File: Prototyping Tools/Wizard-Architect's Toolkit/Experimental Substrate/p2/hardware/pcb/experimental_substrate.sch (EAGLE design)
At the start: 3 parts, among them J1 EURO_POWER

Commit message: Extreme improvements on stripboard v2
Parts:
- added D1, D2: SCHOTTKY_THT, SonicAthame:SCHOTTKY_THT
- added L1, L2: FERRITE_THT, SonicAthame:FERRITE_THT
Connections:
- new net N$10: J1.-12V, L2.P$1
- new net N$11: J1.+12V, L1.P$1
- new net N$8: D1.A, L1.P$2
- new net N$9: D2.C, L2.P$2
- net +12V: now also D1.C; no longer J1.+12V
- net -12V: now also D2.A; no longer J1.-12V
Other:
- note added: "2743005112"
- note added: "ESS106M063AE2EA"
- note added: "SB230TA"
- moved on the sheet: C1, C2
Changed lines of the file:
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@@
 <?xml version="1.0" encoding="utf-8"?>
 <!DOCTYPE eagle SYSTEM "eagle.dtd">
-<eagle version="9.5.0">
+<eagle version="9.6.2">
 <drawing>
 <settings>
@@
 <part name="J1" library="SonicAthame" library_urn="urn:adsk.eagle:library:22327399" deviceset="EURO_POWER" device="" package3d_urn="urn:adsk.eagle:package:26183621/4"/>
 <part name="FRAME1" library="SonicAthame" library_urn="urn:adsk.eagle:library:22327399" deviceset="FRAME_TABL_L" device=""/>
+<part name="D1" library="SonicAthame" library_urn="urn:adsk.eagle:library:22327399" deviceset="SCHOTTKY" device="_THT" package3d_urn="urn:adsk.eagle:package:26423854/3"/>
+<part name="D2" library="SonicAthame" library_urn="urn:adsk.eagle:library:22327399" deviceset="SCHOTTKY" device="_THT" package3d_urn="urn:adsk.eagle:package:26423854/3"/>
+<part name="L1" library="SonicAthame" library_urn="urn:adsk.eagle:library:22327399" deviceset="FERRITE" device="_THT" package3d_urn="urn:adsk.eagle:package:26183824/1"/>
+<part name="L2" library="SonicAthame" library_urn="urn:adsk.eagle:library:22327399" deviceset="FERRITE" device="_THT" package3d_urn="urn:adsk.eagle:package:26183824/1"/>
 </parts>
 <sheets>
 <sheet>
 <plain>
+<text x="205.994" y="128.778" size="1.778" layer="96">SB230TA</text>
+<text x="190.246" y="149.352" size="1.778" layer="96">2743005112</text>
+<text x="236.728" y="145.796" size="1.778" layer="96">ESS106M063AE2EA</text>
 </plain>
 <instances>
-<instance part="C1" gate="G$1" x="203.2" y="147.32" smashed="yes">
-<attribute name="NAME" x="204.216" y="147.955" size="1.778" layer="95"/>
-<attribute name="VALUE" x="204.216" y="143.129" size="1.778" layer="96"/>
-</instance>
-<instance part="C2" gate="G$1" x="203.2" y="132.08" smashed="yes">
-<attribute name="NAME" x="204.216" y="132.715" size="1.778" layer="95"/>
-<attribute name="VALUE" x="204.216" y="127.889" size="1.778" layer="96"/>
-</instance>
-<instance part="SUPPLY1" gate="+12V" x="198.12" y="152.4" smashed="yes">
-<attribute name="VALUE" x="198.12" y="155.321" size="1.778" layer="96" align="bottom-center"/>
-</instance>
-<instance part="SUPPLY2" gate="G$1" x="198.12" y="124.46" smashed="yes">
-<attribute name="VALUE" x="198.12" y="121.666" size="1.778" layer="96" align="top-center"/>
-</instance>
-<instance part="SUPPLY3" gate="PE" x="210.82" y="134.62" smashed="yes"/>
+<instance part="C1" gate="G$1" x="231.14" y="147.32" smashed="yes">
+<attribute name="NAME" x="232.156" y="147.955" size="1.778" layer="95"/>
+<attribute name="VALUE" x="232.156" y="143.129" size="1.778" layer="96"/>
+</instance>
+<instance part="C2" gate="G$1" x="231.14" y="132.08" smashed="yes">
+<attribute name="NAME" x="232.156" y="132.715" size="1.778" layer="95"/>
+<attribute name="VALUE" x="232.156" y="127.889" size="1.778" layer="96"/>
+</instance>
+<instance part="SUPPLY1" gate="+12V" x="226.06" y="152.4" smashed="yes">
+<attribute name="VALUE" x="226.06" y="155.321" size="1.778" layer="96" align="bottom-center"/>
+</instance>
+<instance part="SUPPLY2" gate="G$1" x="226.06" y="124.46" smashed="yes">
+<attribute name="VALUE" x="226.06" y="121.666" size="1.778" layer="96" align="top-center"/>
+</instance>
+<instance part="SUPPLY3" gate="PE" x="238.76" y="134.62" smashed="yes"/>
 <instance part="J1" gate="G$1" x="185.42" y="139.7" smashed="yes">
 <attribute name="NAME" x="177.927" y="147.828" size="1.778" layer="95"/>
-<attribute name="VALUE" x="177.927" y="130.048" size="1.778" layer="95"/>
+<attribute name="VALUE" x="175.387" y="130.048" size="1.778" layer="95"/>
 </instance>
 <instance part="FRAME1" gate="G$1" x="0" y="0" smashed="yes"/>
@@
 <attribute name="REV" x="391.16" y="6.35" size="2.54" layer="94"/>
 </instance>
+<instance part="D1" gate="G$1" x="208.28" y="144.78" smashed="yes">
+<attribute name="NAME" x="205.994" y="146.685" size="1.778" layer="95"/>
+<attribute name="VALUE" x="205.994" y="141.351" size="1.778" layer="96"/>
+</instance>
+<instance part="D2" gate="G$1" x="208.28" y="134.62" smashed="yes" rot="R180">
+<attribute name="NAME" x="205.994" y="136.525" size="1.778" layer="95"/>
+<attribute name="VALUE" x="205.994" y="131.191" size="1.778" layer="96"/>
+</instance>
+<instance part="L1" gate="G$1" x="198.12" y="144.78" smashed="yes">
+<attribute name="NAME" x="194.691" y="146.812" size="1.778" layer="95"/>
+</instance>
+<instance part="L2" gate="G$1" x="198.12" y="134.62" smashed="yes">
+<attribute name="NAME" x="194.691" y="136.652" size="1.778" layer="95"/>
+</instance>
 </instances>
 <busses>
@@
 <net name="+12V" class="0">
 <segment>
-<wire x1="190.5" y1="144.78" x2="198.12" y2="144.78" width="0.1524" layer="91"/>
-<wire x1="198.12" y1="144.78" x2="198.12" y2="149.86" width="0.1524" layer="91"/>
+<wire x1="226.06" y1="144.78" x2="226.06" y2="149.86" width="0.1524" layer="91"/>
 <pinref part="C1" gate="G$1" pin="+"/>
-<wire x1="198.12" y1="149.86" x2="203.2" y2="149.86" width="0.1524" layer="91"/>
+<wire x1="226.06" y1="149.86" x2="231.14" y2="149.86" width="0.1524" layer="91"/>
 <pinref part="SUPPLY1" gate="+12V" pin="+12V"/>
-<junction x="198.12" y="149.86"/>
+<junction x="226.06" y="149.86"/>
+<pinref part="D1" gate="G$1" pin="C"/>
+<wire x1="210.82" y1="144.78" x2="226.06" y2="144.78" width="0.1524" layer="91"/>
+</segment>
+</net>
+<net name="-12V" class="0">
+<segment>
+<wire x1="226.06" y1="134.62" x2="226.06" y2="127" width="0.1524" layer="91"/>
+<pinref part="C2" gate="G$1" pin="-"/>
+<wire x1="226.06" y1="127" x2="231.14" y2="127" width="0.1524" layer="91"/>
+<pinref part="SUPPLY2" gate="G$1" pin="-12V"/>
+<junction x="226.06" y="127"/>
+<pinref part="D2" gate="G$1" pin="A"/>
+<wire x1="210.82" y1="134.62" x2="226.06" y2="134.62" width="0.1524" layer="91"/>
+</segment>
+</net>
+<net name="GND" class="0">
+<segment>
+<wire x1="190.5" y1="139.7" x2="231.14" y2="139.7" width="0.1524" layer="91"/>
+<pinref part="C1" gate="G$1" pin="-"/>
+<wire x1="231.14" y1="139.7" x2="231.14" y2="142.24" width="0.1524" layer="91"/>
+<pinref part="C2" gate="G$1" pin="+"/>
+<wire x1="231.14" y1="139.7" x2="231.14" y2="134.62" width="0.1524" layer="91"/>
+<junction x="231.14" y="139.7"/>
+<pinref part="SUPPLY3" gate="PE" pin="GND"/>
+<wire x1="231.14" y1="139.7" x2="238.76" y2="139.7" width="0.1524" layer="91"/>
+<wire x1="238.76" y1="139.7" x2="238.76" y2="137.16" width="0.1524" layer="91"/>
+<pinref part="J1" gate="G$1" pin="GND"/>
+</segment>
+</net>
+<net name="N$8" class="0">
+<segment>
+<pinref part="D1" gate="G$1" pin="A"/>
+<wire x1="203.2" y1="144.78" x2="205.74" y2="144.78" width="0.1524" layer="91"/>
+<pinref part="L1" gate="G$1" pin="P$2"/>
+</segment>
+</net>
+<net name="N$9" class="0">
+<segment>
+<pinref part="D2" gate="G$1" pin="C"/>
+<wire x1="205.74" y1="134.62" x2="203.2" y2="134.62" width="0.1524" layer="91"/>
+<pinref part="L2" gate="G$1" pin="P$2"/>
+</segment>
+</net>
+<net name="N$10" class="0">
+<segment>
+<pinref part="J1" gate="G$1" pin="-12V"/>
+<wire x1="193.04" y1="134.62" x2="190.5" y2="134.62" width="0.1524" layer="91"/>
+<pinref part="L2" gate="G$1" pin="P$1"/>
+</segment>
+</net>
+<net name="N$11" class="0">
+<segment>
 <pinref part="J1" gate="G$1" pin="+12V"/>
-</segment>
-</net>
-<net name="-12V" class="0">
-<segment>
-<wire x1="190.5" y1="134.62" x2="198.12" y2="134.62" width="0.1524" layer="91"/>
-<wire x1="198.12" y1="134.62" x2="198.12" y2="127" width="0.1524" layer="91"/>
-<pinref part="C2" gate="G$1" pin="-"/>
-<wire x1="198.12" y1="127" x2="203.2" y2="127" width="0.1524" layer="91"/>
-<pinref part="SUPPLY2" gate="G$1" pin="-12V"/>
-<junction x="198.12" y="127"/>
-<pinref part="J1" gate="G$1" pin="-12V"/>
-</segment>
-</net>
-<net name="GND" class="0">
-<segment>
-<wire x1="190.5" y1="139.7" x2="203.2" y2="139.7" width="0.1524" layer="91"/>
-<pinref part="C1" gate="G$1" pin="-"/>
-<wire x1="203.2" y1="139.7" x2="203.2" y2="142.24" width="0.1524" layer="91"/>
-<pinref part="C2" gate="G$1" pin="+"/>
-<wire x1="203.2" y1="139.7" x2="203.2" y2="134.62" width="0.1524" layer="91"/>
-<junction x="203.2" y="139.7"/>
-<pinref part="SUPPLY3" gate="PE" pin="GND"/>
-<wire x1="203.2" y1="139.7" x2="210.82" y2="139.7" width="0.1524" layer="91"/>
-<wire x1="210.82" y1="139.7" x2="210.82" y2="137.16" width="0.1524" layer="91"/>
-<pinref part="J1" gate="G$1" pin="GND"/>
-</segment>
-</net>
+<wire x1="193.04" y1="144.78" x2="190.5" y2="144.78" width="0.1524" layer="91"/>
+<pinref part="L1" gate="G$1" pin="P$1"/>
+</segment>
+</net>

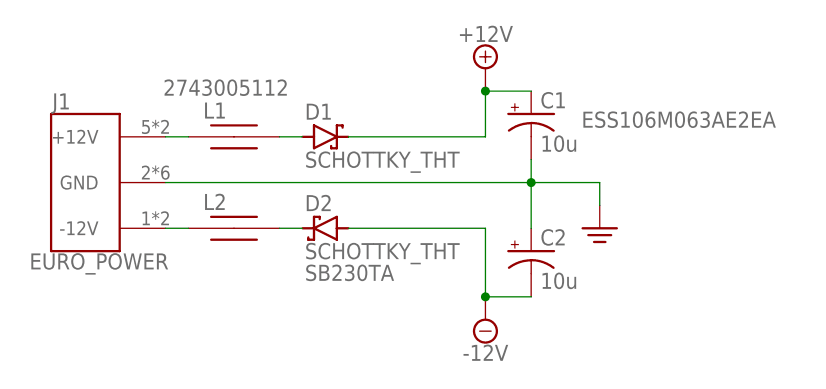
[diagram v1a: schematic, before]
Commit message: Cleaner schematic layout
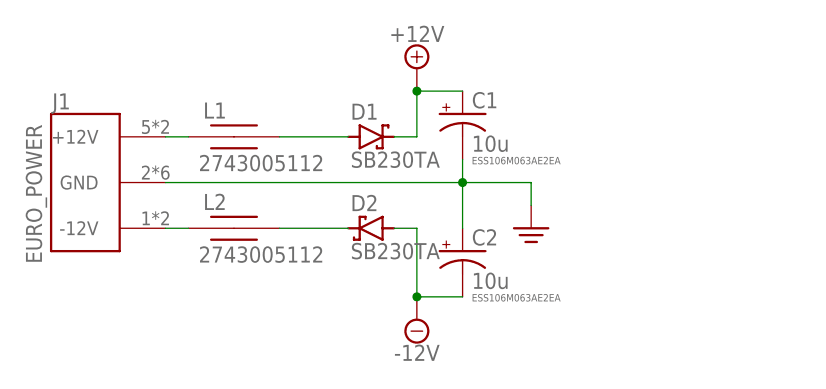
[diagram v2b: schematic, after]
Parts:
- D1, D2: value SCHOTTKY_THT -> SB230TA
- L1, L2: value FERRITE_THT -> 2743005112
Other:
- note removed: "2743005112"
- note removed: "SB230TA"
- moved on the sheet: C1, C2, D1, D2
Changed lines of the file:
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@@
 <part name="J1" library="SonicAthame" library_urn="urn:adsk.eagle:library:22327399" deviceset="EURO_POWER" device="" package3d_urn="urn:adsk.eagle:package:26183621/4"/>
 <part name="FRAME1" library="SonicAthame" library_urn="urn:adsk.eagle:library:22327399" deviceset="FRAME_TABL_L" device=""/>
-<part name="D1" library="SonicAthame" library_urn="urn:adsk.eagle:library:22327399" deviceset="SCHOTTKY" device="_THT" package3d_urn="urn:adsk.eagle:package:26423854/3"/>
-<part name="D2" library="SonicAthame" library_urn="urn:adsk.eagle:library:22327399" deviceset="SCHOTTKY" device="_THT" package3d_urn="urn:adsk.eagle:package:26423854/3"/>
-<part name="L1" library="SonicAthame" library_urn="urn:adsk.eagle:library:22327399" deviceset="FERRITE" device="_THT" package3d_urn="urn:adsk.eagle:package:26183824/1"/>
-<part name="L2" library="SonicAthame" library_urn="urn:adsk.eagle:library:22327399" deviceset="FERRITE" device="_THT" package3d_urn="urn:adsk.eagle:package:26183824/1"/>
+<part name="D1" library="SonicAthame" library_urn="urn:adsk.eagle:library:22327399" deviceset="SCHOTTKY" device="_THT" package3d_urn="urn:adsk.eagle:package:26423854/3" value="SB230TA"/>
+<part name="D2" library="SonicAthame" library_urn="urn:adsk.eagle:library:22327399" deviceset="SCHOTTKY" device="_THT" package3d_urn="urn:adsk.eagle:package:26423854/3" value="SB230TA"/>
+<part name="L1" library="SonicAthame" library_urn="urn:adsk.eagle:library:22327399" deviceset="FERRITE" device="_THT" package3d_urn="urn:adsk.eagle:package:26183824/1" value="2743005112"/>
+<part name="L2" library="SonicAthame" library_urn="urn:adsk.eagle:library:22327399" deviceset="FERRITE" device="_THT" package3d_urn="urn:adsk.eagle:package:26183824/1" value="2743005112"/>
 </parts>
 <sheets>
 <sheet>
 <plain>
-<text x="205.994" y="128.778" size="1.778" layer="96">SB230TA</text>
-<text x="190.246" y="149.352" size="1.778" layer="96">2743005112</text>
-<text x="236.728" y="145.796" size="1.778" layer="96">ESS106M063AE2EA</text>
+<text x="224.536" y="141.732" size="0.8128" layer="96">ESS106M063AE2EA</text>
+<text x="224.536" y="126.492" size="0.8128" layer="96">ESS106M063AE2EA</text>
 </plain>
 <instances>
-<instance part="C1" gate="G$1" x="231.14" y="147.32" smashed="yes">
-<attribute name="NAME" x="232.156" y="147.955" size="1.778" layer="95"/>
-<attribute name="VALUE" x="232.156" y="143.129" size="1.778" layer="96"/>
+<instance part="C1" gate="G$1" x="223.52" y="147.32" smashed="yes">
+<attribute name="NAME" x="224.536" y="147.955" size="1.778" layer="95"/>
+<attribute name="VALUE" x="224.536" y="143.129" size="1.778" layer="96"/>
 </instance>
-<instance part="C2" gate="G$1" x="231.14" y="132.08" smashed="yes">
-<attribute name="NAME" x="232.156" y="132.715" size="1.778" layer="95"/>
-<attribute name="VALUE" x="232.156" y="127.889" size="1.778" layer="96"/>
+<instance part="C2" gate="G$1" x="223.52" y="132.08" smashed="yes">
+<attribute name="NAME" x="224.536" y="132.715" size="1.778" layer="95"/>
+<attribute name="VALUE" x="224.536" y="127.889" size="1.778" layer="96"/>
 </instance>
-<instance part="SUPPLY1" gate="+12V" x="226.06" y="152.4" smashed="yes">
-<attribute name="VALUE" x="226.06" y="155.321" size="1.778" layer="96" align="bottom-center"/>
+<instance part="SUPPLY1" gate="+12V" x="218.44" y="152.4" smashed="yes">
+<attribute name="VALUE" x="218.44" y="155.321" size="1.778" layer="96" align="bottom-center"/>
 </instance>
-<instance part="SUPPLY2" gate="G$1" x="226.06" y="124.46" smashed="yes">
-<attribute name="VALUE" x="226.06" y="121.666" size="1.778" layer="96" align="top-center"/>
+<instance part="SUPPLY2" gate="G$1" x="218.44" y="124.46" smashed="yes">
+<attribute name="VALUE" x="218.44" y="121.666" size="1.778" layer="96" align="top-center"/>
 </instance>
-<instance part="SUPPLY3" gate="PE" x="238.76" y="134.62" smashed="yes"/>
+<instance part="SUPPLY3" gate="PE" x="231.14" y="134.62" smashed="yes"/>
 <instance part="J1" gate="G$1" x="185.42" y="139.7" smashed="yes">
 <attribute name="NAME" x="177.927" y="147.828" size="1.778" layer="95"/>
-<attribute name="VALUE" x="175.387" y="130.048" size="1.778" layer="95"/>
+<attribute name="VALUE" x="176.784" y="130.683" size="1.778" layer="95" rot="R90"/>
 </instance>
 <instance part="FRAME1" gate="G$1" x="0" y="0" smashed="yes"/>
@@
 <attribute name="REV" x="391.16" y="6.35" size="2.54" layer="94"/>
 </instance>
-<instance part="D1" gate="G$1" x="208.28" y="144.78" smashed="yes">
-<attribute name="NAME" x="205.994" y="146.685" size="1.778" layer="95"/>
-<attribute name="VALUE" x="205.994" y="141.351" size="1.778" layer="96"/>
+<instance part="D1" gate="G$1" x="213.36" y="144.78" smashed="yes">
+<attribute name="NAME" x="211.074" y="146.685" size="1.778" layer="95"/>
+<attribute name="VALUE" x="211.074" y="141.351" size="1.778" layer="96"/>
 </instance>
-<instance part="D2" gate="G$1" x="208.28" y="134.62" smashed="yes" rot="R180">
-<attribute name="NAME" x="205.994" y="136.525" size="1.778" layer="95"/>
-<attribute name="VALUE" x="205.994" y="131.191" size="1.778" layer="96"/>
+<instance part="D2" gate="G$1" x="213.36" y="134.62" smashed="yes" rot="R180">
+<attribute name="NAME" x="211.074" y="136.525" size="1.778" layer="95"/>
+<attribute name="VALUE" x="211.074" y="131.191" size="1.778" layer="96"/>
 </instance>
 <instance part="L1" gate="G$1" x="198.12" y="144.78" smashed="yes">
 <attribute name="NAME" x="194.691" y="146.812" size="1.778" layer="95"/>
+<attribute name="VALUE" x="194.183" y="140.97" size="1.778" layer="95"/>
 </instance>
 <instance part="L2" gate="G$1" x="198.12" y="134.62" smashed="yes">
 <attribute name="NAME" x="194.691" y="136.652" size="1.778" layer="95"/>
+<attribute name="VALUE" x="194.183" y="130.81" size="1.778" layer="95"/>
 </instance>
 </instances>
@@
 <net name="+12V" class="0">
 <segment>
-<wire x1="226.06" y1="144.78" x2="226.06" y2="149.86" width="0.1524" layer="91"/>
+<wire x1="218.44" y1="144.78" x2="218.44" y2="149.86" width="0.1524" layer="91"/>
 <pinref part="C1" gate="G$1" pin="+"/>
-<wire x1="226.06" y1="149.86" x2="231.14" y2="149.86" width="0.1524" layer="91"/>
+<wire x1="218.44" y1="149.86" x2="223.52" y2="149.86" width="0.1524" layer="91"/>
 <pinref part="SUPPLY1" gate="+12V" pin="+12V"/>
-<junction x="226.06" y="149.86"/>
+<junction x="218.44" y="149.86"/>
 <pinref part="D1" gate="G$1" pin="C"/>
-<wire x1="210.82" y1="144.78" x2="226.06" y2="144.78" width="0.1524" layer="91"/>
+<wire x1="215.9" y1="144.78" x2="218.44" y2="144.78" width="0.1524" layer="91"/>
 </segment>
 </net>
 <net name="-12V" class="0">
 <segment>
-<wire x1="226.06" y1="134.62" x2="226.06" y2="127" width="0.1524" layer="91"/>
+<wire x1="218.44" y1="134.62" x2="218.44" y2="127" width="0.1524" layer="91"/>
 <pinref part="C2" gate="G$1" pin="-"/>
-<wire x1="226.06" y1="127" x2="231.14" y2="127" width="0.1524" layer="91"/>
+<wire x1="218.44" y1="127" x2="223.52" y2="127" width="0.1524" layer="91"/>
 <pinref part="SUPPLY2" gate="G$1" pin="-12V"/>
-<junction x="226.06" y="127"/>
+<junction x="218.44" y="127"/>
 <pinref part="D2" gate="G$1" pin="A"/>
-<wire x1="210.82" y1="134.62" x2="226.06" y2="134.62" width="0.1524" layer="91"/>
+<wire x1="215.9" y1="134.62" x2="218.44" y2="134.62" width="0.1524" layer="91"/>
 </segment>
 </net>
 <net name="GND" class="0">
 <segment>
-<wire x1="190.5" y1="139.7" x2="231.14" y2="139.7" width="0.1524" layer="91"/>
+<wire x1="190.5" y1="139.7" x2="223.52" y2="139.7" width="0.1524" layer="91"/>
 <pinref part="C1" gate="G$1" pin="-"/>
-<wire x1="231.14" y1="139.7" x2="231.14" y2="142.24" width="0.1524" layer="91"/>
+<wire x1="223.52" y1="139.7" x2="223.52" y2="142.24" width="0.1524" layer="91"/>
 <pinref part="C2" gate="G$1" pin="+"/>
-<wire x1="231.14" y1="139.7" x2="231.14" y2="134.62" width="0.1524" layer="91"/>
-<junction x="231.14" y="139.7"/>
+<wire x1="223.52" y1="139.7" x2="223.52" y2="134.62" width="0.1524" layer="91"/>
+<junction x="223.52" y="139.7"/>
 <pinref part="SUPPLY3" gate="PE" pin="GND"/>
-<wire x1="231.14" y1="139.7" x2="238.76" y2="139.7" width="0.1524" layer="91"/>
-<wire x1="238.76" y1="139.7" x2="238.76" y2="137.16" width="0.1524" layer="91"/>
+<wire x1="223.52" y1="139.7" x2="231.14" y2="139.7" width="0.1524" layer="91"/>
+<wire x1="231.14" y1="139.7" x2="231.14" y2="137.16" width="0.1524" layer="91"/>
 <pinref part="J1" gate="G$1" pin="GND"/>
 </segment>
@@
 <segment>
 <pinref part="D1" gate="G$1" pin="A"/>
-<wire x1="203.2" y1="144.78" x2="205.74" y2="144.78" width="0.1524" layer="91"/>
+<wire x1="203.2" y1="144.78" x2="210.82" y2="144.78" width="0.1524" layer="91"/>
 <pinref part="L1" gate="G$1" pin="P$2"/>
 </segment>
@@
 <segment>
 <pinref part="D2" gate="G$1" pin="C"/>
-<wire x1="205.74" y1="134.62" x2="203.2" y2="134.62" width="0.1524" layer="91"/>
+<wire x1="210.82" y1="134.62" x2="203.2" y2="134.62" width="0.1524" layer="91"/>
 <pinref part="L2" gate="G$1" pin="P$2"/>
 </segment>

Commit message: Updated stripboard with design block
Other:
- note added: "Eurorack Power Input"
- moved on the sheet: C1, C2, D1, D2, J1, L1, L2
